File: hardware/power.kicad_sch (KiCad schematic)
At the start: 48 parts, among them J1 USB4085-GF-A, J2 Batteries, J3 Conn_01x02, J4 Conn_01x02, J5 Conn_01x02, J6 Conn_01x02, Q1 PMOS, Q2 PMOS, Q3 PMOS, U1 USBLC6-2SC6, U2 TLV76733DGNR

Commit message: HW: Layout power section
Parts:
- renumbered F2 to F1, F1 to F2
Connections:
- net at F2.1, J1.A4 (VBUS), J1.A9 (VBUS)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: now also U1.5 (VBUS)
- net at C6.1, F2.2, FB2.1: no longer U1.5 (VBUS)
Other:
- moved on the sheet: F2, U1
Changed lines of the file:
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@@
 	)
 	(junction
+		(at 116.84 66.04)
+		(diameter 0)
+		(color 0 0 0 0)
+	)
+	(junction
 		(at 116.84 96.52)
 		(diameter 0)
@@
 	)
 	(junction
-		(at 116.84 66.04)
+		(at 96.52 66.04)
 		(diameter 0)
 		(color 0 0 0 0)
@@
 	)
 	(junction
-		(at 100.33 66.04)
-		(diameter 0)
-		(color 0 0 0 0)
-	)
-	(junction
 		(at 170.18 88.9)
 		(diameter 0)
@@
 	)
 	(junction
-		(at 100.33 96.52)
-		(diameter 0)
-		(color 0 0 0 0)
-	)
-	(junction
 		(at 91.44 185.42)
 		(diameter 0)
@@
 	)
 	(junction
+		(at 96.52 96.52)
+		(diameter 0)
+		(color 0 0 0 0)
+	)
+	(junction
 		(at 204.47 148.59)
 		(diameter 0)
@@
 	(wire
 		(pts
-			(xy 100.33 66.04) (xy 100.33 76.2)
+			(xy 96.52 66.04) (xy 96.52 76.2)
 		)
 		(stroke
@@
 	(wire
 		(pts
-			(xy 100.33 66.04) (xy 116.84 66.04)
+			(xy 229.87 41.91) (xy 231.14 41.91)
 		)
 		(stroke
@@
 	(wire
 		(pts
-			(xy 229.87 41.91) (xy 231.14 41.91)
+			(xy 80.01 193.04) (xy 91.44 193.04)
 		)
 		(stroke
@@
 	(wire
 		(pts
-			(xy 80.01 193.04) (xy 91.44 193.04)
+			(xy 78.74 96.52) (xy 85.09 96.52)
 		)
 		(stroke
@@
 	(wire
 		(pts
-			(xy 78.74 96.52) (xy 85.09 96.52)
+			(xy 163.83 148.59) (xy 172.72 148.59)
 		)
 		(stroke
@@
 	(wire
 		(pts
-			(xy 163.83 148.59) (xy 172.72 148.59)
+			(xy 68.58 185.42) (xy 80.01 185.42)
 		)
 		(stroke
@@
 	(wire
 		(pts
-			(xy 68.58 185.42) (xy 80.01 185.42)
+			(xy 96.52 66.04) (xy 102.87 66.04)
 		)
 		(stroke
@@
 	(wire
 		(pts
-			(xy 100.33 96.52) (xy 116.84 96.52)
+			(xy 146.05 49.53) (xy 146.05 57.15)
 		)
 		(stroke
@@
 	(wire
 		(pts
-			(xy 146.05 49.53) (xy 146.05 57.15)
+			(xy 96.52 96.52) (xy 116.84 96.52)
 		)
 		(stroke
@@
 	(wire
 		(pts
-			(xy 88.9 66.04) (xy 100.33 66.04)
+			(xy 229.87 66.04) (xy 238.76 66.04)
 		)
 		(stroke
@@
 	(wire
 		(pts
-			(xy 229.87 66.04) (xy 238.76 66.04)
+			(xy 194.31 130.81) (xy 207.01 130.81)
 		)
 		(stroke
@@
 	(wire
 		(pts
-			(xy 194.31 130.81) (xy 207.01 130.81)
+			(xy 76.2 81.28) (xy 91.44 81.28)
 		)
 		(stroke
@@
 	(wire
 		(pts
-			(xy 76.2 81.28) (xy 95.25 81.28)
+			(xy 128.27 57.15) (xy 133.35 57.15)
 		)
 		(stroke
@@
 	(wire
 		(pts
-			(xy 128.27 57.15) (xy 133.35 57.15)
+			(xy 168.91 123.19) (xy 181.61 123.19)
 		)
 		(stroke
@@
 	(wire
 		(pts
-			(xy 168.91 123.19) (xy 181.61 123.19)
+			(xy 182.88 96.52) (xy 191.77 96.52)
 		)
 		(stroke
@@
 	(wire
 		(pts
-			(xy 182.88 96.52) (xy 191.77 96.52)
+			(xy 102.87 57.15) (xy 114.3 57.15)
 		)
 		(stroke
@@
 	(wire
 		(pts
-			(xy 102.87 57.15) (xy 114.3 57.15)
+			(xy 96.52 88.9) (xy 96.52 96.52)
 		)
 		(stroke
@@
 	(wire
 		(pts
-			(xy 100.33 88.9) (xy 100.33 96.52)
+			(xy 110.49 66.04) (xy 116.84 66.04)
 		)
 		(stroke
@@
 	(wire
 		(pts
-			(xy 90.17 83.82) (xy 95.25 83.82)
+			(xy 90.17 83.82) (xy 91.44 83.82)
 		)
 		(stroke
@@
 	(wire
 		(pts
-			(xy 87.63 96.52) (xy 100.33 96.52)
+			(xy 87.63 96.52) (xy 96.52 96.52)
 		)
 		(stroke
@@
 	(wire
 		(pts
-			(xy 81.28 66.04) (xy 76.2 66.04)
+			(xy 76.2 66.04) (xy 96.52 66.04)
 		)
 		(stroke
@@
 	(global_label "USB_DP"
 		(shape bidirectional)
-		(at 105.41 83.82 0)
+		(at 101.6 83.82 0)
 		(fields_autoplaced yes)
 		(effects
@@
 		)
 		(property "Intersheetrefs" "${INTERSHEET_REFS}"
-			(at 116.0111 83.82 0)
+			(at 112.2011 83.82 0)
 			(effects
 				(font
@@
 	(global_label "USB_DN"
 		(shape bidirectional)
-		(at 105.41 81.28 0)
+		(at 101.6 81.28 0)
 		(fields_autoplaced yes)
 		(effects
@@
 		)
 		(property "Intersheetrefs" "${INTERSHEET_REFS}"
-			(at 116.0716 81.28 0)
+			(at 112.2616 81.28 0)
 			(effects
 				(font
@@
 	(symbol
 		(lib_id "Device:Polyfuse")
-		(at 85.09 66.04 90)
+		(at 106.68 66.04 90)
 		(unit 1)
 		(exclude_from_sim no)
@@
 		(on_board yes)
 		(dnp no)
-		(property "Reference" "F1"
-			(at 85.09 63.754 90)
+		(property "Reference" "F2"
+			(at 106.68 63.754 90)
 			(effects
 				(font
@@
 		)
 		(property "Value" "2A"
-			(at 85.09 68.326 90)
+			(at 106.68 68.326 90)
 			(effects
 				(font
@@
 		)
 		(property "Footprint" "Fuse:Fuse_0805_2012Metric"
-			(at 90.17 64.77 0)
+			(at 111.76 64.77 0)
 			(effects
 				(font
@@
 		)
 		(property "Datasheet" "~"
-			(at 85.09 66.04 0)
+			(at 106.68 66.04 0)
 			(effects
 				(font
@@
 		)
 		(property "Description" "Resettable fuse, polymeric positive temperature coefficient"
-			(at 85.09 66.04 0)
+			(at 106.68 66.04 0)
 			(effects
 				(font
@@
 		)
 		(property "Digi-Key Part Number" "13-SMD0805B110TFCT-ND"
-			(at 85.09 66.04 0)
+			(at 106.68 66.04 0)
 			(effects
 				(font
@@
 		)
 		(property "Manufacturer" "YAGEO"
-			(at 85.09 66.04 0)
+			(at 106.68 66.04 0)
 			(effects
 				(font
@@
 		)
 		(property "Manufacturer Part Number" "SMD0805B110TF"
-			(at 85.09 66.04 0)
+			(at 106.68 66.04 0)
 			(effects
 				(font
@@
 			(project "iida_devkit"
 				(path "/b12a6e25-97fb-4aba-bc96-af8db389bb9a/8a51e004-740e-440f-9bfb-b035bcbeb0d2"
-					(reference "F1")
+					(reference "F2")
 					(unit 1)
 				)
@@
 		(on_board yes)
 		(dnp no)
-		(property "Reference" "F2"
+		(property "Reference" "F1"
 			(at 102.87 39.624 90)
 			(effects
@@
 			(project "iida_devkit"
 				(path "/b12a6e25-97fb-4aba-bc96-af8db389bb9a/8a51e004-740e-440f-9bfb-b035bcbeb0d2"
-					(reference "F2")
+					(reference "F1")
 					(unit 1)
 				)
@@
 	(symbol
 		(lib_id "Power_Protection:USBLC6-2SC6")
-		(at 100.33 81.28 0)
+		(at 96.52 81.28 0)
 		(unit 1)
 		(exclude_from_sim no)
@@
 		(dnp no)
 		(property "Reference" "U1"
-			(at 102.108 76.962 0)
+			(at 98.298 76.962 0)
 			(effects
 				(font
@@
 		)
 		(property "Value" "USBLC6-2SC6"
-			(at 108.204 88.138 0)
+			(at 104.394 88.138 0)
 			(effects
 				(font
@@
 		)
 		(property "Footprint" "Package_TO_SOT_SMD:SOT-23-6"
-			(at 100.33 93.98 0)
+			(at 96.52 93.98 0)
 			(effects
 				(font
@@
 		)
 		(property "Datasheet" "https://www.st.com/resource/en/datasheet/usblc6-2.pdf"
-			(at 105.41 72.39 0)
+			(at 101.6 72.39 0)
 			(effects
 				(font
@@
 		)
 		(property "Description" "Very low capacitance ESD protection diode, 2 data-line, SOT-23-6"
-			(at 100.33 81.28 0)
+			(at 96.52 81.28 0)
 			(effects
 				(font
@@
 		)
 		(property "Manufacturer" "STMicroelectronics"
-			(at 100.33 81.28 90)
+			(at 96.52 81.28 90)
 			(effects
 				(font
@@
 		)
 		(property "Manufacturer Part Number" "USBLC6-2SC6"
-			(at 100.33 81.28 90)
+			(at 96.52 81.28 90)
 			(effects
 				(font
@@
 		)
 		(property "Digi-Key Part Number" "497-5235-1-ND"
-			(at 100.33 81.28 90)
+			(at 96.52 81.28 90)
 			(effects
 				(font

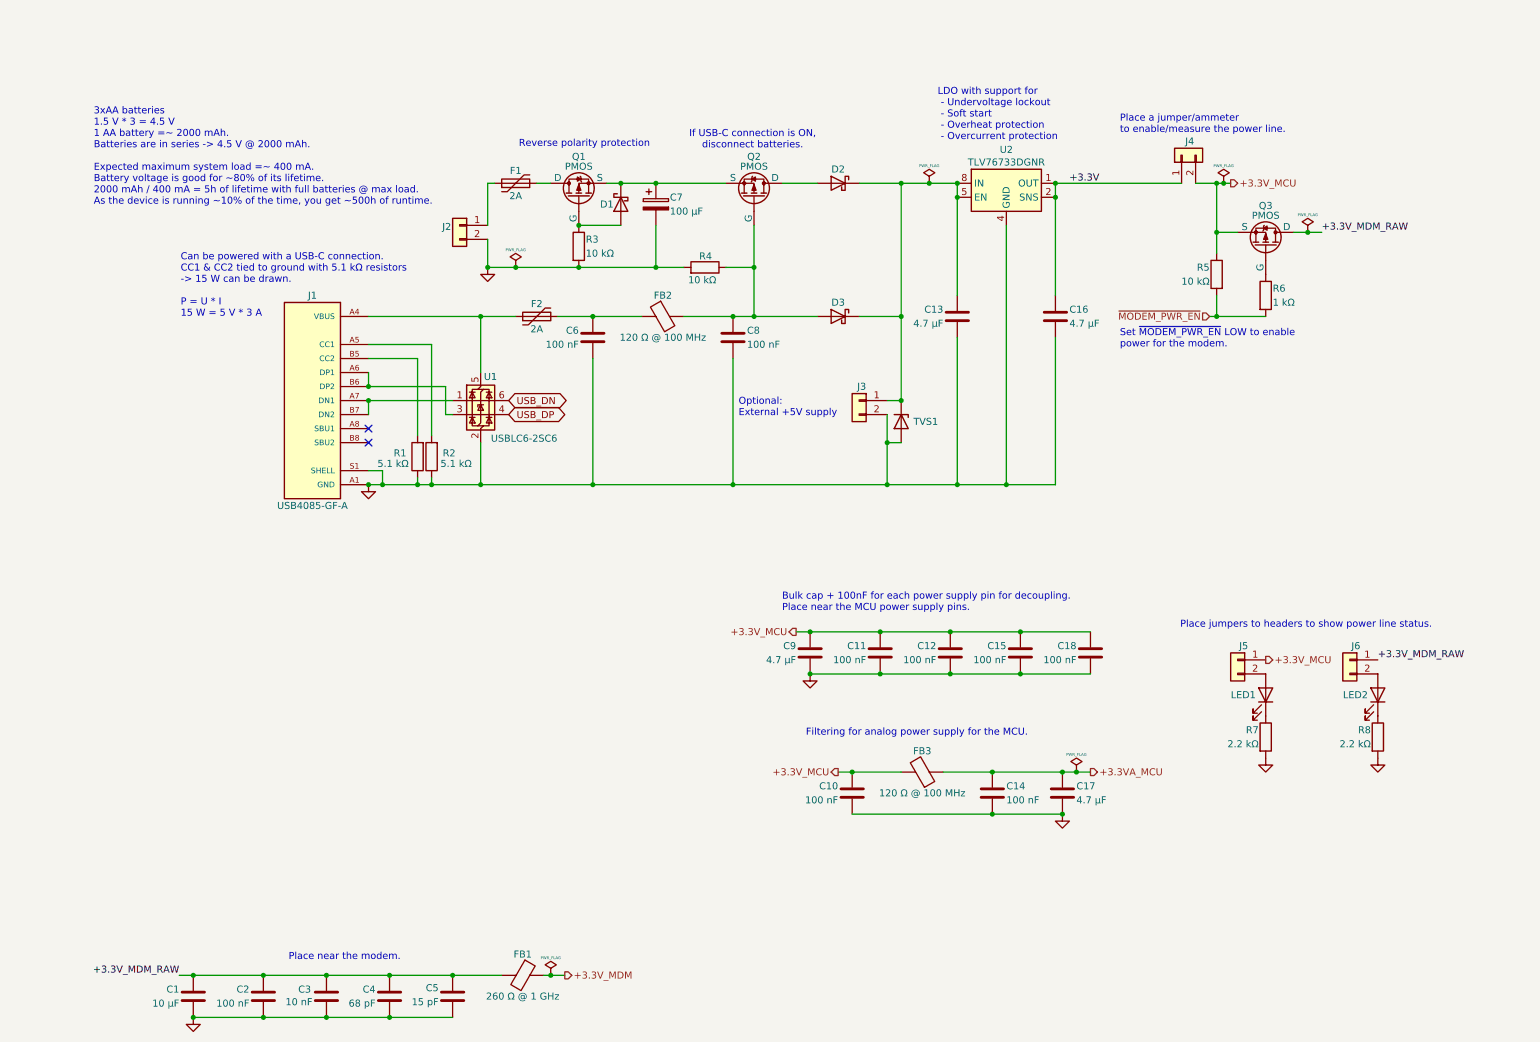
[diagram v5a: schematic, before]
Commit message: HW: Rework power section
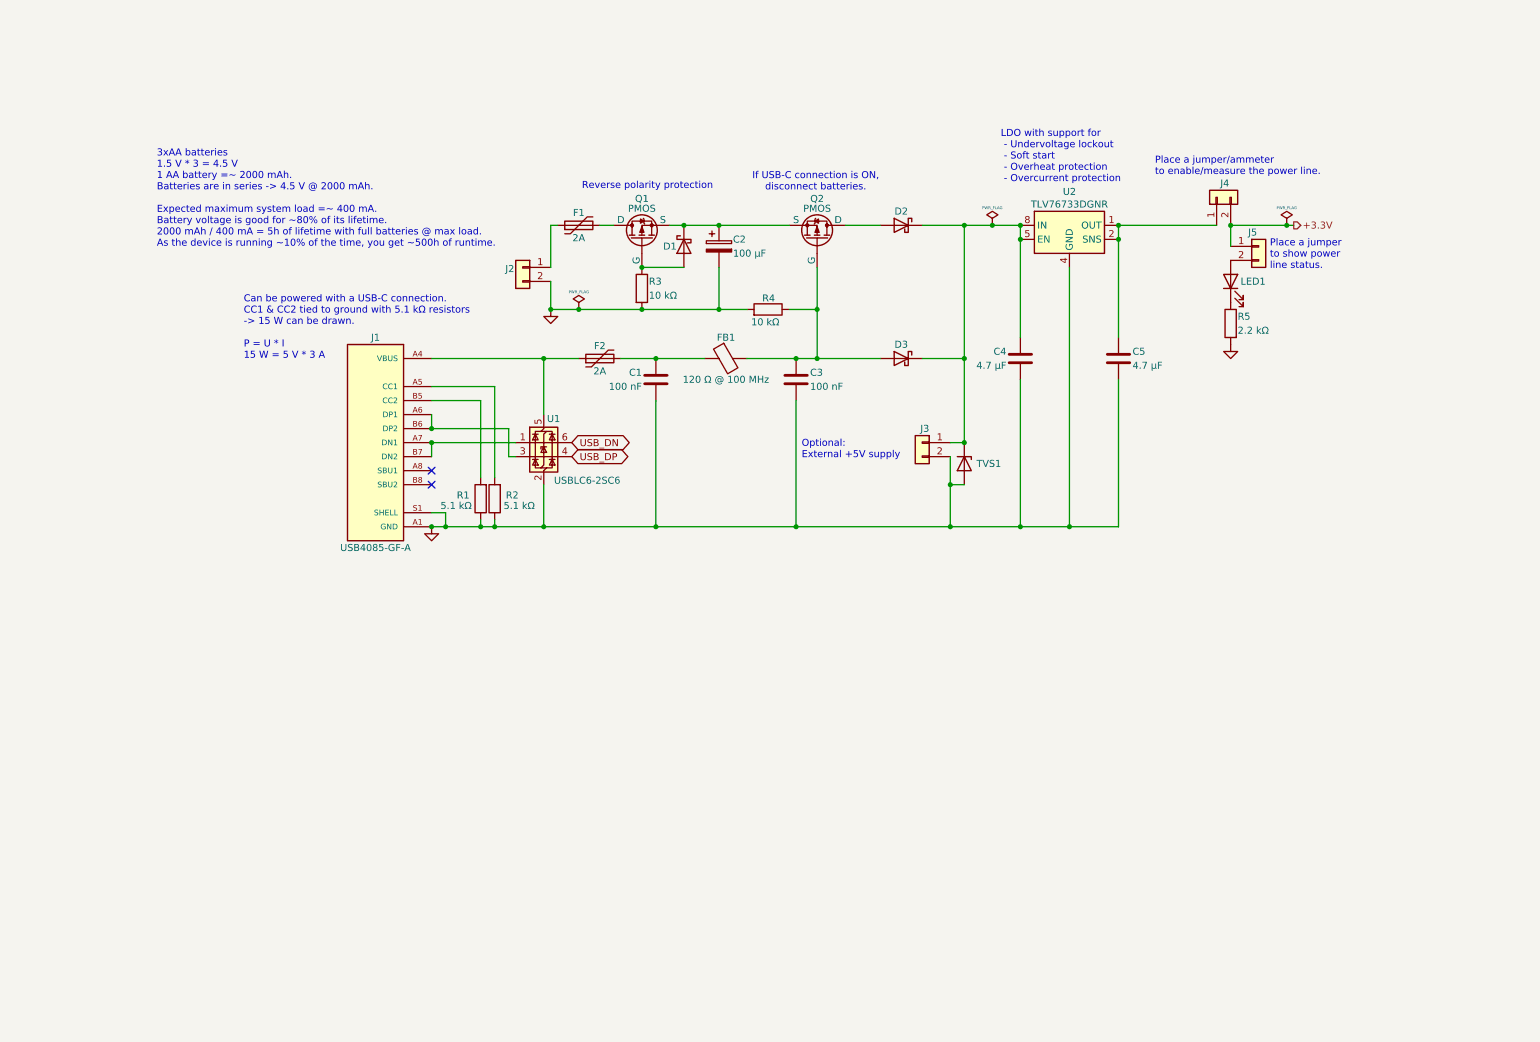
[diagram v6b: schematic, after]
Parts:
- removed C1: 10 µF, Capacitor_SMD:C_0603_1608Metric, symbol Device:C
- removed C10, C11, C12, C14, C15, C18, C2: 100 nF, perfect_footprints:0402_1005_perfect, symbol Device:C
- removed C17, C9: 4.7 µF, Capacitor_SMD:C_0603_1608Metric, symbol Device:C
- removed C3: 10 nF, perfect_footprints:0402_1005_perfect, symbol Device:C
- removed C4: 68 pF, perfect_footprints:0402_1005_perfect, symbol Device:C
- removed C5: 15 pF, perfect_footprints:0402_1005_perfect, symbol Device:C
- removed FB1: 260 Ω @ 1 GHz, Resistor_SMD:R_0603_1608Metric, symbol Device:FerriteBead
- removed FB3: 120 Ω @ 100 MHz, Resistor_SMD:R_0603_1608Metric, symbol Device:FerriteBead
- removed J6: Conn_01x02, Connector_PinHeader_2.54mm:PinHeader_1x02_P2.54mm_Vertical, symbol Connector_Generic:Conn_01x02
- removed LED2: LS T67K-K1L2-1-0-2-R18-Z, LED_SMD:LED_PLCC_2835, symbol Device:LED
- removed Q3: PMOS, Package_TO_SOT_SMD:SOT-23-3, symbol Simulation_SPICE:PMOS
- removed R5: 10 kΩ, perfect_footprints:0402_1005_perfect, symbol Device:R
- removed R6: 1 kΩ, perfect_footprints:0402_1005_perfect, symbol Device:R
- removed R8: 2.2 kΩ, perfect_footprints:0402_1005_perfect, symbol Device:R
- renumbered C6 to C1, C7 to C2, C8 to C3, C13 to C4, C16 to C5, FB2 to FB1, R7 to R5
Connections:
- net +3.3V_MCU is gone; now on net +3.3V: J4.2 (Pin_2), J5.1 (Pin_1)
- net +3.3V: no longer C5.1, J4.1 (Pin_1), U2.1 (OUT), U2.2 (SNS)
- new net: C5.1, J4.1 (Pin_1), U2.1 (OUT), U2.2 (SNS)
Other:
- note added: "Place a jumper to show power line status."
- note removed: "Bulk cap + 100nF for each power supply pin for decoupling. Place near the MCU power supply pins."
- note removed: "Filtering for analog power supply for the MCU."
- note removed: "Place jumpers to headers to show power line status."
- note removed: "Place near the modem."
- note removed: "Set ~{MODEM_PWR_EN} LOW to enable power for the modem."
- moved on the sheet: C1, C2, C3, C4, C5, D1, D2, D3, F1, F2, FB1, J1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

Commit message: HW: Initial layout and routing done
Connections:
- net USB_DP_IN: now reaches J1.A6 (DP1), J1.B6 (DP2), U1.3 (I/O2)
- net USB_DN_IN: now reaches J1.A7 (DN1), J1.B7 (DN2), U1.1 (I/O1)
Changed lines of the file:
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@@
 	(title_block
 		(title "Iida devkit")
-		(date "2024-09-08")
+		(date "2024-09-10")
 		(rev "v4.0.0")
 	)
@@
 		)
 	)
+	(label "USB_DN_IN"
+		(at 88.9 88.9 0)
+		(fields_autoplaced yes)
+		(effects
+			(font
+				(size 1.27 1.27)
+			)
+			(justify left bottom)
+		)
+	)
+	(label "USB_DP_IN"
+		(at 88.9 86.36 0)
+		(fields_autoplaced yes)
+		(effects
+			(font
+				(size 1.27 1.27)
+			)
+			(justify left bottom)
+		)
+	)

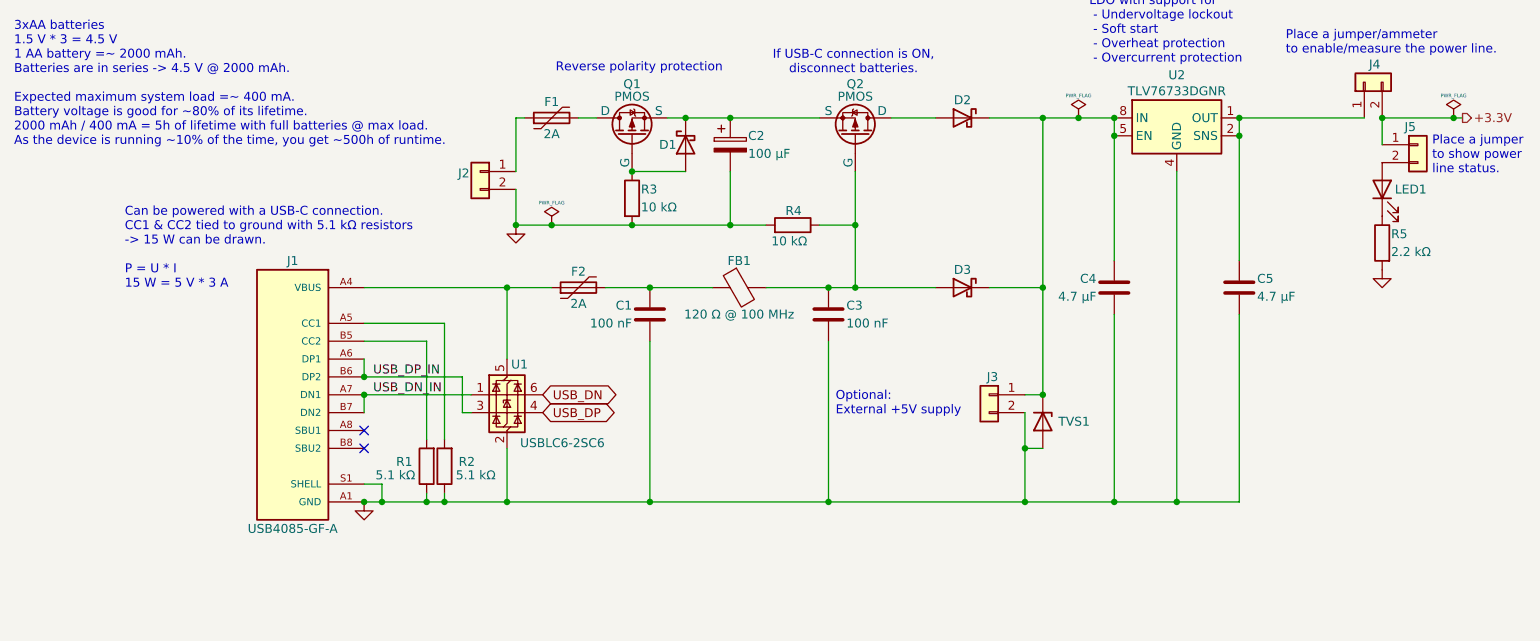
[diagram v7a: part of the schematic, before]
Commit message: HW: Update schematic
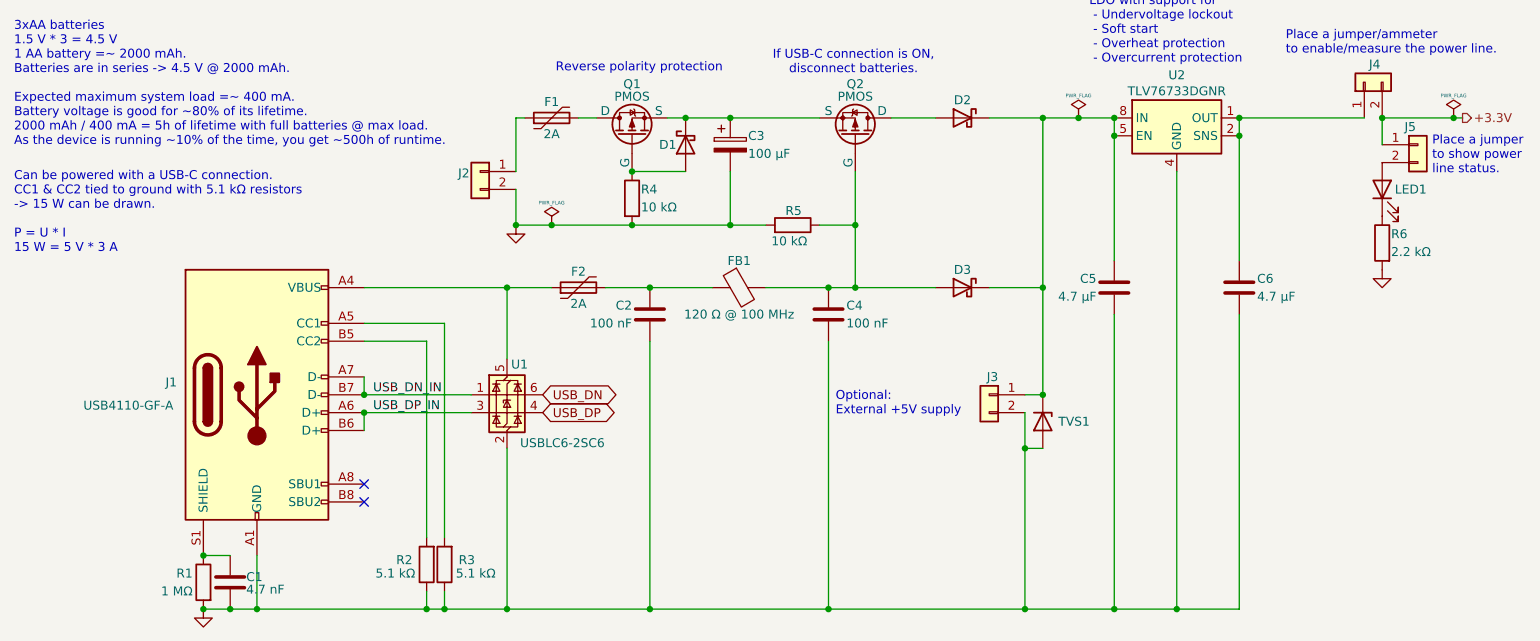
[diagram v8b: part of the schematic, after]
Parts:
- removed J1: USB4085-GF-A, USB4105-GF-A:USB4085-GF-A, symbol USB4085-GF-A:USB4085-GF-A
- added C1: 4.7 nF, perfect_footprints:0402_1005_perfect, symbol Device:C
- added J1: USB4110-GF-A, Connector_USB:USB_C_Receptacle_GCT_USB4110, symbol Connector:USB_C_Receptacle_USB2.0_16P
- added R1: 1 MΩ, Resistor_SMD:R_0805_2012Metric, symbol Device:R
- renumbered C1 to C2, C2 to C3, C3 to C4, C4 to C5, C5 to C6, R1 to R2, R2 to R3, R3 to R4, R4 to R5, R5 to R6
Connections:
- net GND: now also C1.2, J1.A1 (GND), J1.A12 (GND), J1.B1 (GND), J1.B12 (GND), R1.2
- net USB_DN_IN: now also J1.A7 (D-), J1.B7 (D-)
- net USB_DP_IN: now also J1.A6 (D+), J1.B6 (D+)
- net at F2.1, U1.5 (VBUS): now also J1.A4 (VBUS), J1.A9 (VBUS), J1.B4 (VBUS), J1.B9 (VBUS)
- net at R3.2: now also J1.A5 (CC1)
- net at R2.2: now also J1.B5 (CC2)
- new net: C1.1, J1.S1 (SHIELD), R1.1
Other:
- moved on the sheet: R2, R3
